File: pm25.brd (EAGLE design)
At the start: 55.9 x 33 mm, 33 parts, among them J1 CON-0024, Q1 TRANSISTOR-NPN-40V-0.2A-SOT23, Q2 TR-0001, U1 IC-0010, U2 CCS811B-JOPD500, U3 POWER-SWITCH-SIP32509DT', U4 SI7021-A20-GM1R

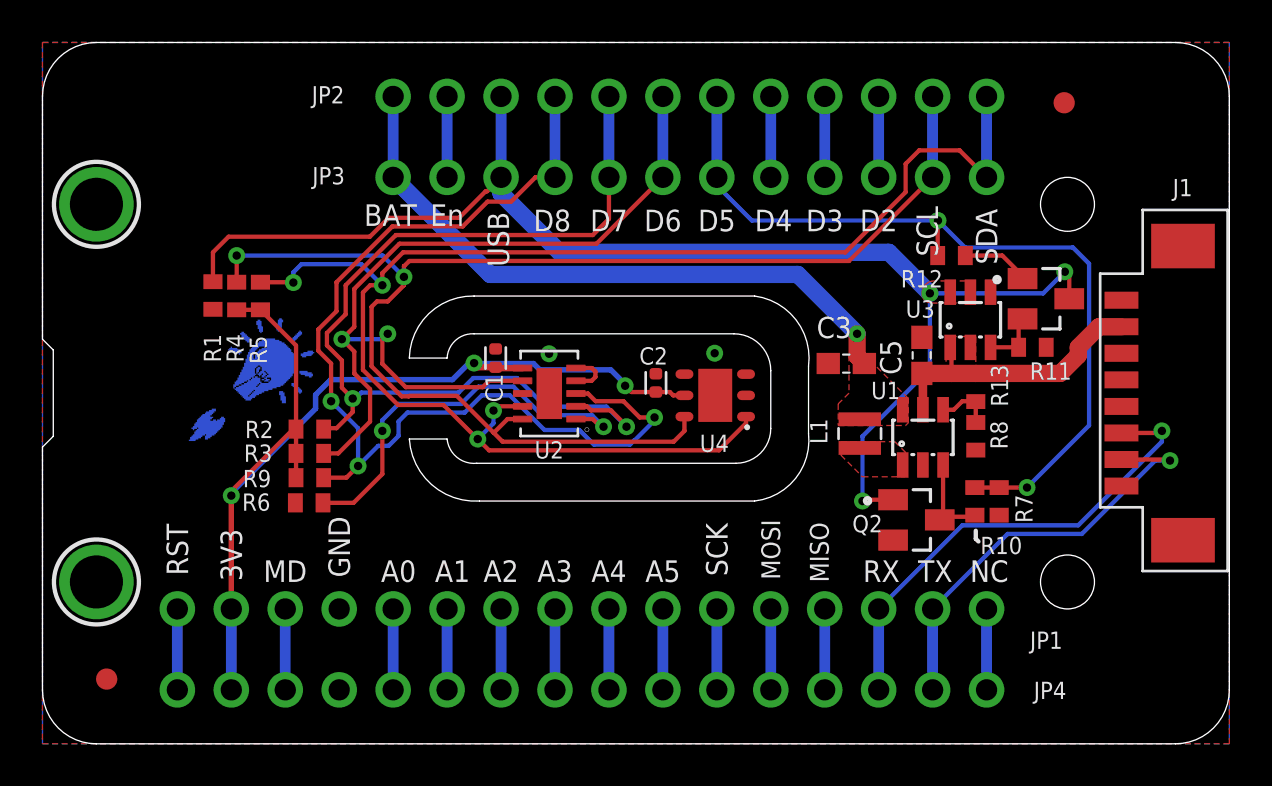
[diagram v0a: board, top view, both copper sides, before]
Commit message: Slight hardware update. Substitute MCP1640 on U1 Add L2 Add TP1
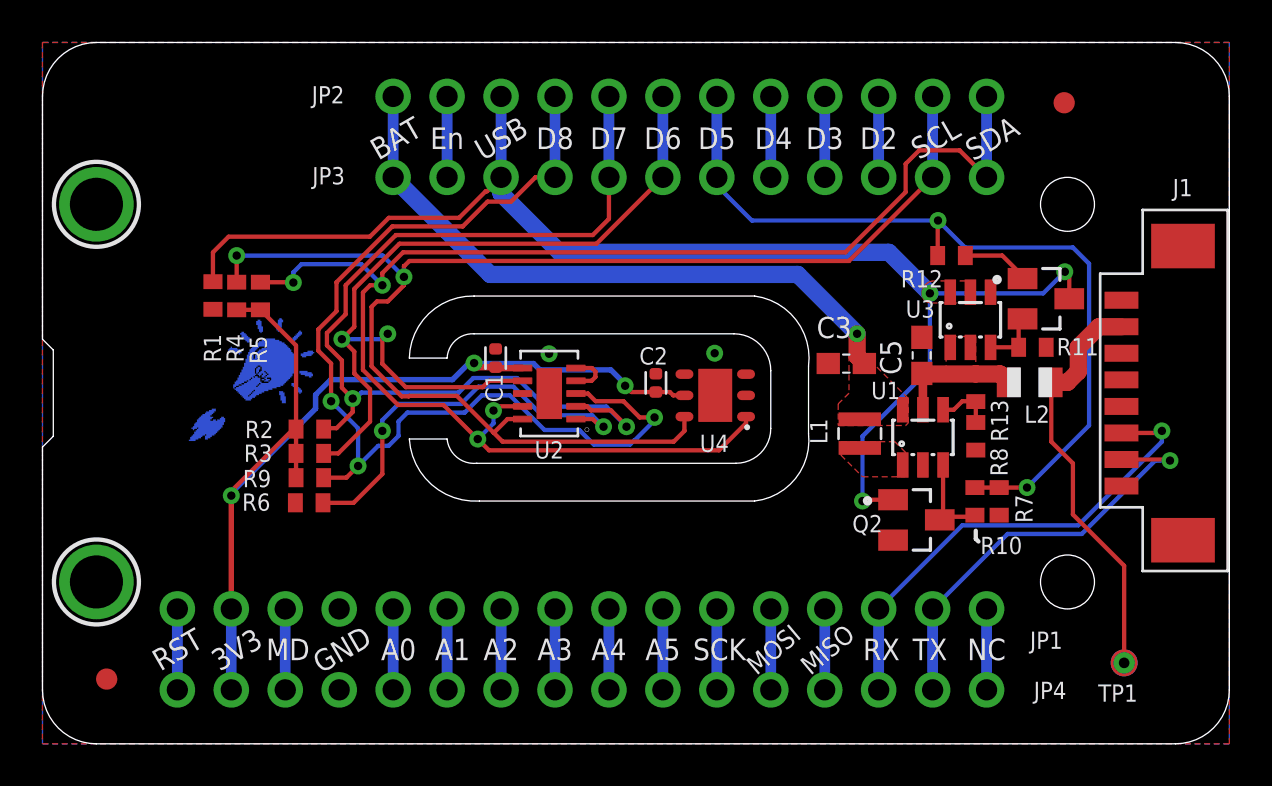
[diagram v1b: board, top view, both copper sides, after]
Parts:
- added L2: 2k, wolff-den:R0805
- added TP1: TP, wolff-den:TP-1P27
- U1: value IC-0010 -> POWER-VREG-FB-EN-SW-350MA
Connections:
- new net V5V0_BEAD: C5.1, L2.1, R13.2, U1.5, U3.1, U3.2
- net V5V0_HAT: now also L2.2, TP1.P$1, TP1.P$2, TP1.TP; no longer C5.1, R13.2, U1.5, U3.1, U3.2
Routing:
- net V5V0_HAT: track 13.6 -> 19.7 mm
- net V5V0_BEAD: track 0.00 -> 5.94 mm
- added copper zone on layer 1, net V5V0_BEAD
- removed copper zone on layer 1, net V5V0_HAT
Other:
- board text added: ">LAST_DATE_TIME"
- board text added: "BRD-0010-02"
- board text removed: "BRD-0010-01"

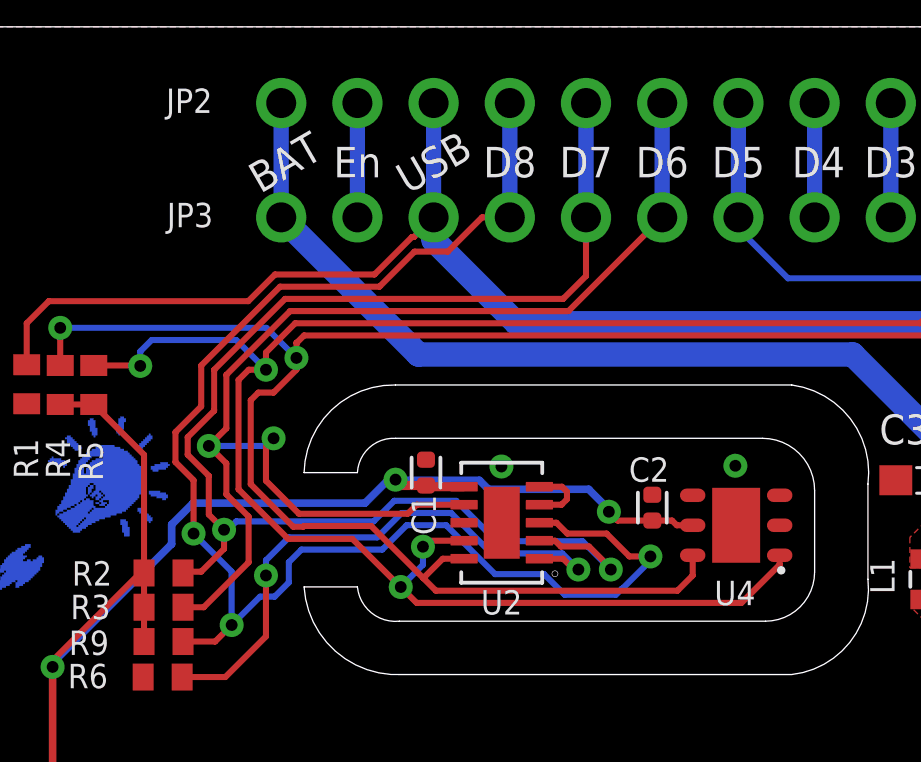
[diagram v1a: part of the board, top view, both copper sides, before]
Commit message: Replacing connection from D7 with D5 (so the LED isn't always on)
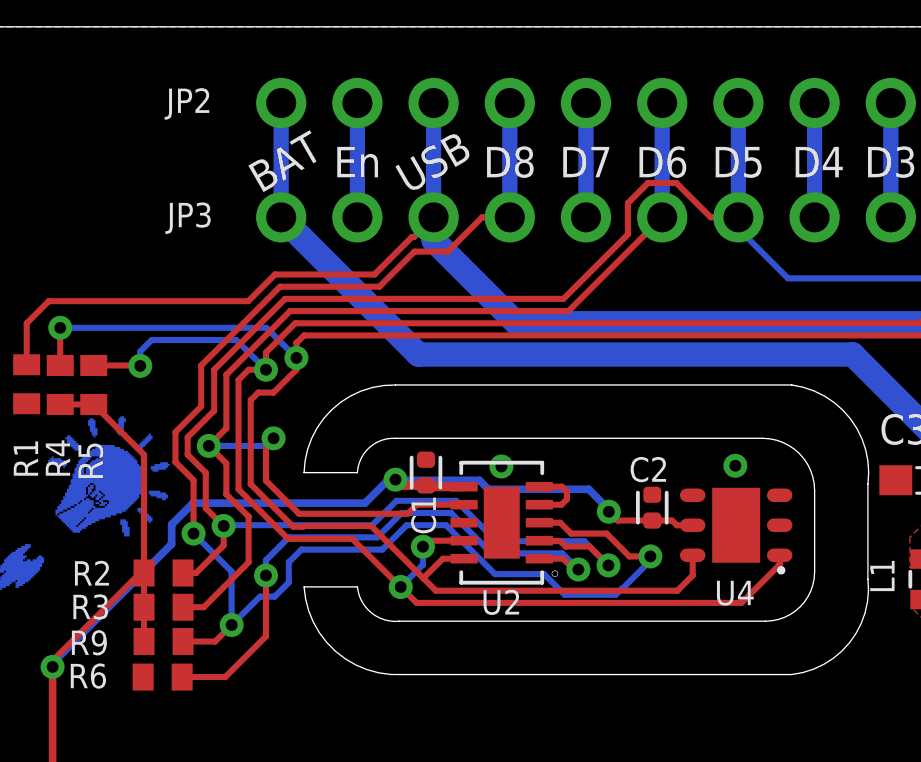
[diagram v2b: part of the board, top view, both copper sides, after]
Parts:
- added PCB1: PCB-PS-CCS811-SI7021, wolff-den:PLACEHOLDER
- U3: value POWER-SWITCH-SIP32509DT' -> POWER-SWITCH-SIP32509DT
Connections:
- net D5: now also R2.1, U2.2
- net D7: no longer R2.1, U2.2
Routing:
- net D5: track 39.1 -> 85.4 mm, vias 2 -> 4
- net D7: track 45.0 -> 3.81 mm, vias 2 -> 0

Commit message: Fixing issue with intermittent BOOST/USB control.
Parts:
- added Q3: TR-0003, wolff-den:SOT23
- Q1: value TRANSISTOR-NPN-40V-0.2A-SOT23 -> TR-0001
- R11: value 100k -> 1k
- R12: value 1k -> 100k
- moved Q1 7.78 mm to (39.5, 21.7), turned to 0 degrees
- moved R11 2.11 mm to (47.8, 16.9), turned to 90 degrees
- moved L2 1.09 mm to (45.8, 16.1), turned to 270 degrees
- moved R12 0.40 mm to (42.7, 22.6), turned to 180 degrees
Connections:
- net D5: now also Q1.1; no longer R12.1
- net GND: now also J1.1, Q1.2; no longer J1.8
- net N$3: now also Q1.3, Q3.1, R12.1; no longer Q1.2, R11.2, U3.3
- net N$7: now also Q3.3, R11.2, U3.3; no longer Q1.1, R12.2
- net RX: now also J1.3; no longer J1.6
- net TX: now also J1.2; no longer J1.7
- net V5V0_HAT: now also J1.7; no longer J1.2
- net VBUS: now also Q3.2, R12.2; no longer Q1.3
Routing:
- net N$3: track 2.74 -> 10.9 mm
- net TX: track 20.3 -> 26.2 mm
- net RX: track 22.9 -> 26.3 mm
- net V5V0_HAT: track 19.7 -> 16.3 mm
- net VBUS: track 64.0 -> 63.2 mm
- net N$7: track 3.22 -> 3.89 mm
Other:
- board text added: "BRD-0010-03"
- board text removed: "BRD-0010-02"

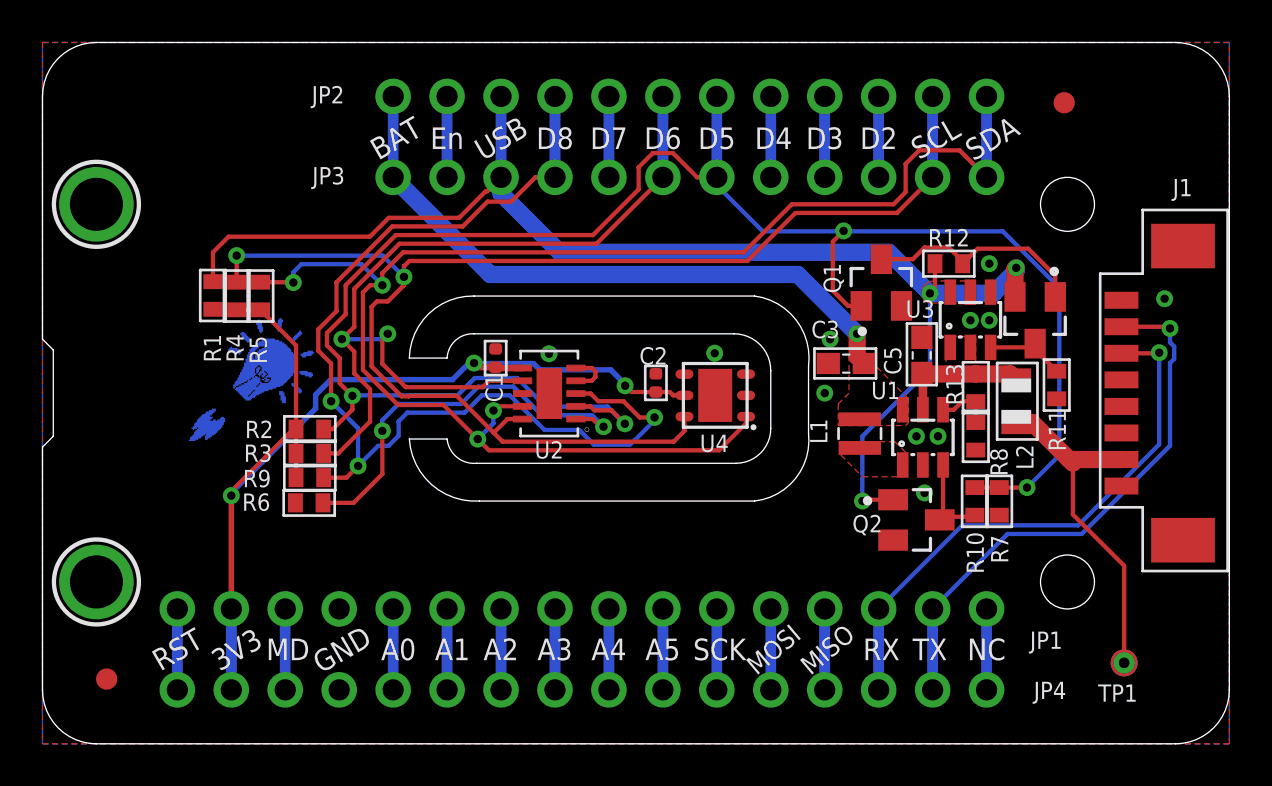
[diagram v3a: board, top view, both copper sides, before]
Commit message: Updating board based on recommendations
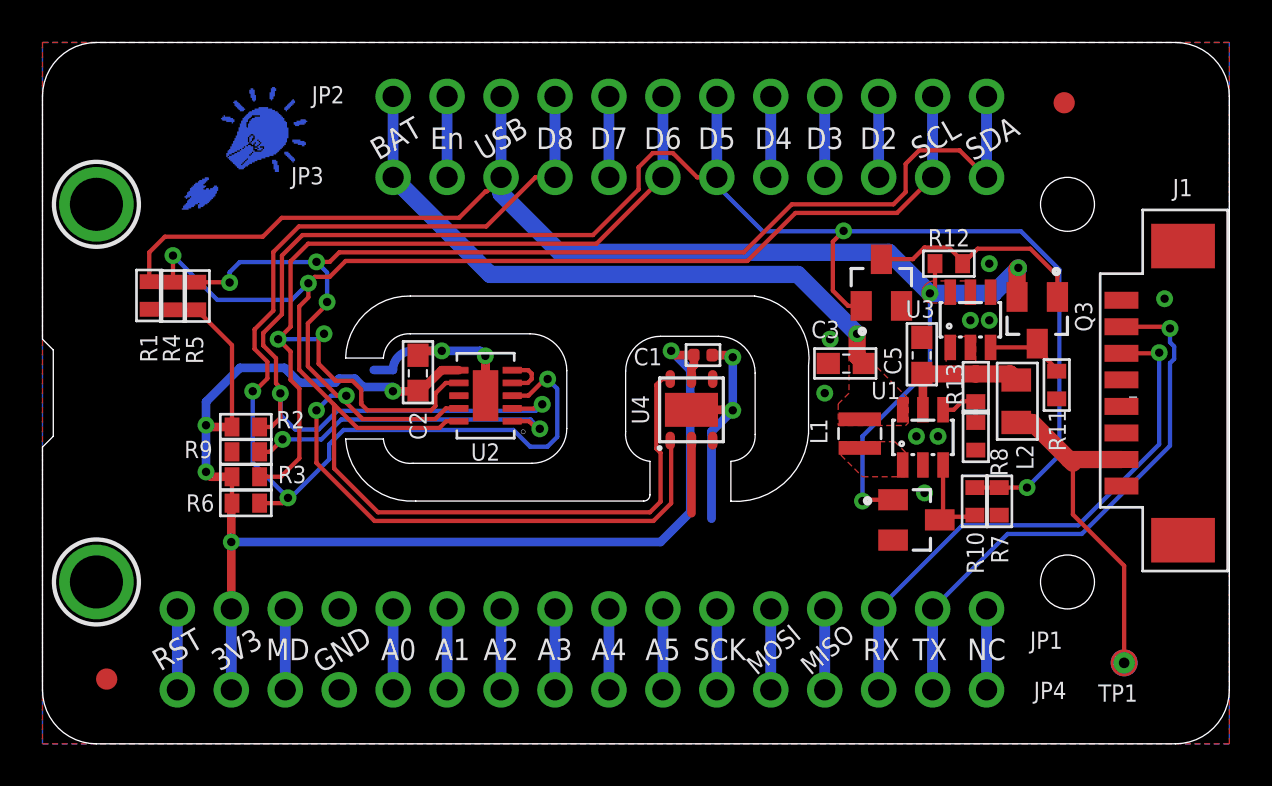
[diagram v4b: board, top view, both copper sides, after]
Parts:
- added U$1: (no value), wolff-den:LOGO-CIRCUITDOJO-BULB
- added U$2: (no value), wolff-den:LOGO-CIRCUITDOJO
- C2: value 0.1u -> 4.7u; device wolff-den:CAPC1005X55N -> wolff-den:C0603
- R2, R3, R6, R9: value 100k -> 4.7k
- moved C2 11.2 mm to (17.7, 17.4)
- moved C1 9.76 mm to (31.1, 18.3), turned to 0 degrees
- moved R9 3.83 mm to (9.57, 13.7)
- moved R6 3.25 mm to (9.57, 11.3)
- moved R3 3.21 mm to (9.57, 12.6)
- moved R2 3.02 mm to (9.57, 14.9)
- moved U2 3.00 mm to (20.9, 16.4)
- moved R1 3.00 mm to (5.03, 21.1)
- moved R4 3.00 mm to (6.14, 21.1)
- moved R5 3.00 mm to (7.26, 21.1)
- moved U4 1.31 mm to (30.6, 15.7), turned to 90 degrees
- moved Q3 0.10 mm to (46.8, 19.9)
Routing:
- net GND: track 0.00 -> 24.4 mm, vias 11 -> 13
- net +3V3: track 50.8 -> 69.5 mm, vias 3 -> 5
- net SCL: track 64.4 -> 82.9 mm
- net SDA: track 71.6 -> 84.5 mm, vias 4 -> 5
- net D6: track 41.3 -> 47.7 mm
- net N$4: track 19.2 -> 15.5 mm
- net D8: track 49.4 -> 53.0 mm
- net VBUS: track 63.2 -> 66.2 mm
- net D5: track 85.8 -> 88.7 mm
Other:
- outline, holes or cut-outs redrawn
- board text added: "BRD-0010-04"
- board text removed: "BRD-0010-03"

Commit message: Fixing load switch option
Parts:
- U3: value POWER-SWITCH-SIP32509DT -> POWER-SWITCH-SIP32508-SO23-6
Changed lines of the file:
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@@
 <drawing>
 <settings>
-<setting alwaysvectorfont="yes"/>
+<setting alwaysvectorfont="no"/>
 <setting keepoldvectorfont="yes"/>
 <setting verticaltext="up"/>
@@
 <attribute name="VALUE" x="45.72" y="5.715" size="0.4064" layer="27" ratio="10" rot="R180"/>
 </element>
-<element name="U1" library="wolff-den" library_urn="urn:adsk.eagle:library:6370453" package="SOT23-6" package3d_urn="urn:adsk.eagle:package:5807329/2" value="POWER-VREG-FB-EN-SW-350MA" x="41.4528" y="14.4272" smashed="yes">
+<element name="U1" library="wolff-den" library_urn="urn:adsk.eagle:library:6370453" package="SOT23-6" package3d_urn="urn:adsk.eagle:package:5807329/3" value="POWER-VREG-FB-EN-SW-350MA" x="41.4528" y="14.4272" smashed="yes">
 <attribute name="DIGIKEYPN" value="MCP1640BT-I/CHYCT-ND" x="41.4528" y="14.4272" size="1.778" layer="27" display="off"/>
 <attribute name="MPN" value="MCP1640BT-I/CHY" x="41.4528" y="14.4272" size="1.778" layer="27" display="off"/>
@@
 <attribute name="DIGIKEYPN" value="1727-1142-1-ND" x="41.148" y="10.541" size="1.778" layer="27" rot="R270" display="off"/>
 <attribute name="MPN" value="BSS138P,215" x="41.148" y="10.541" size="1.778" layer="27" rot="R270" display="off"/>
+<attribute name="NAME" x="40.753" y="10.946" size="0.8128" layer="51" rot="R270"/>
 <attribute name="NAME" x="38.1254" y="9.9568" size="0.8128" layer="25"/>
-<attribute name="NAME" x="40.753" y="10.946" size="0.8128" layer="51" rot="R270"/>
 <attribute name="TEMPHIGH" value="150" x="41.148" y="10.541" size="1.778" layer="27" rot="R270" display="off"/>
 <attribute name="TEMPLOW" value="-55" x="41.148" y="10.541" size="1.778" layer="27" rot="R270" display="off"/>
@@
 <attribute name="VENDOR" value="Yageo" x="7.2616" y="21.082" size="1.778" layer="27" rot="R270" display="off"/>
 </element>
-<element name="U3" library="wolff-den" library_urn="urn:adsk.eagle:library:6370453" package="SOT23-6" package3d_urn="urn:adsk.eagle:package:5807329/2" value="POWER-SWITCH-SIP32509DT" x="43.688" y="19.9644" smashed="yes">
+<element name="U3" library="wolff-den" library_urn="urn:adsk.eagle:library:6370453" package="SOT23-6" package3d_urn="urn:adsk.eagle:package:5807329/3" value="POWER-SWITCH-SIP32508-SO23-6" x="43.688" y="19.9644" smashed="yes">
 <attribute name="DESC" value="IC LOAD SWITCH SOT23-6" x="43.688" y="19.9644" size="1.778" layer="27" display="off"/>
-<attribute name="DIGIKEYPN" value="SIP32509DT-T1-GE3CT-ND" x="43.688" y="19.9644" size="1.778" layer="27" display="off"/>
-<attribute name="MPN" value="SIP32509DT-T1-GE3" x="43.688" y="19.9644" size="1.778" layer="27" display="off"/>
+<attribute name="DIGIKEYPN" value="SIP32508DT-T1-GE3CT-ND" x="43.688" y="19.9644" size="1.778" layer="27" display="off"/>
+<attribute name="MPN" value="SIP32508DT-T1-GE3" x="43.688" y="19.9644" size="1.778" layer="27" display="off"/>
 <attribute name="NAME" x="40.64" y="20.066" size="0.8128" layer="25"/>
 </element>
@@
 <attribute name="DIGIKEYPN" value="1727-1142-1-ND" x="39.497" y="21.717" size="1.778" layer="27" display="off"/>
 <attribute name="MPN" value="BSS138P,215" x="39.497" y="21.717" size="1.778" layer="27" display="off"/>
+<attribute name="NAME" x="39.092" y="21.322" size="0.8128" layer="51"/>
 <attribute name="NAME" x="37.592" y="21.209" size="0.8128" layer="25" rot="R90"/>
-<attribute name="NAME" x="39.092" y="21.322" size="0.8128" layer="51"/>
 <attribute name="TEMPHIGH" value="150" x="39.497" y="21.717" size="1.778" layer="27" display="off"/>
 <attribute name="TEMPLOW" value="-55" x="39.497" y="21.717" size="1.778" layer="27" display="off"/>
@@
 <attribute name="DIGIKEYPN" value="BSS84-FDICT-ND" x="46.836" y="19.939" size="1.778" layer="27" rot="R180" display="off"/>
 <attribute name="MPN" value="BSS84-7-F" x="46.836" y="19.939" size="1.778" layer="27" rot="R180" display="off"/>
+<attribute name="NAME" x="48.614" y="20.828" size="0.8128" layer="25" rot="R270"/>
 <attribute name="NAME" x="47.241" y="20.334" size="0.8128" layer="51" rot="R180"/>
-<attribute name="NAME" x="48.614" y="20.828" size="0.8128" layer="25" rot="R270"/>
 <attribute name="TEMPHIGH" value="150" x="46.836" y="19.939" size="1.778" layer="27" rot="R180" display="off"/>
 <attribute name="TEMPLOW" value="-55" x="46.836" y="19.939" size="1.778" layer="27" rot="R180" display="off"/>
@@
 <wire x1="17.8862" y1="18.5" x2="18.8" y2="18.5" width="0.4064" layer="1"/>
 <via x="18.8" y="18.5" extent="1-16" drill="0.3937"/>
+<wire x1="52.832" y1="20.955" x2="50.8" y2="20.885" width="0" layer="19" extent="1-1"/>
+<wire x1="47.752" y1="16.241" x2="50.8" y2="20.885" width="0" layer="19" extent="1-1"/>
+<wire x1="43.942" y1="13.828" x2="47.752" y2="16.241" width="0" layer="19" extent="1-1"/>
+<wire x1="42.164" y1="14.478" x2="43.942" y2="13.828" width="0" layer="19" extent="1-1"/>
+<wire x1="41.148" y1="14.478" x2="42.164" y2="14.478" width="0" layer="19" extent="1-1"/>
+<wire x1="41.4528" y1="13.1272" x2="41.148" y2="14.478" width="0" layer="19" extent="1-1"/>
+<wire x1="41.529" y1="11.811" x2="41.4528" y2="13.1272" width="0" layer="19" extent="1-1"/>
+<wire x1="40.048" y1="9.591" x2="41.529" y2="11.811" width="0" layer="19" extent="1-1"/>
+<wire x1="45.042" y1="10.765" x2="43.942" y2="13.828" width="0" layer="19" extent="1-1"/>
+<wire x1="41.402" y1="19.138" x2="41.148" y2="14.478" width="0" layer="19" extent="1-1"/>
+<wire x1="40.447" y1="20.617" x2="41.402" y2="19.138" width="0" layer="19" extent="1-1"/>
+<wire x1="43.688" y1="19.939" x2="41.402" y2="19.138" width="0" layer="19" extent="1-1"/>
+<wire x1="44.577" y1="19.939" x2="43.688" y2="19.939" width="0" layer="19" extent="1-1"/>
+<wire x1="44.638" y1="21.2644" x2="44.577" y2="19.939" width="0" layer="19" extent="1-1"/>
+<wire x1="44.577" y1="22.606" x2="44.638" y2="21.2644" width="0" layer="19" extent="1-1"/>
+<wire x1="37.084" y1="19.05" x2="40.447" y2="20.617" width="0" layer="19" extent="1-1"/>
+<wire x1="36.996" y1="17.907" x2="37.084" y2="19.05" width="0" layer="19" extent="1-1"/>
+<wire x1="36.83" y1="16.51" x2="36.996" y2="17.907" width="0" layer="19" extent="1-1"/>
+<wire x1="32.5" y1="15.7" x2="36.83" y2="16.51" width="0" layer="19" extent="1-1"/>
+<wire x1="30.5558" y1="10.8558" x2="31.5" y2="10.6" width="0" layer="19" extent="1-16"/>
+<wire x1="20.861" y1="16.3908" x2="30.5558" y2="15.724" width="0" layer="19" extent="1-1"/>
+<wire x1="8.923" y1="13.746" x2="15.6" y2="17.6" width="0" layer="19" extent="1-16"/>
+<wire x1="5.0264" y1="20.4574" x2="8.923" y2="13.746" width="0" layer="19" extent="1-1"/>
+<wire x1="13.97" y1="6.35" x2="8.923" y2="13.746" width="0" layer="19" extent="1-1"/>
+<wire x1="13.97" y1="2.54" x2="13.97" y2="6.35" width="0" layer="19" extent="1-1"/>
 </signal>
 <signal name="MOSI">
@@
 <wire x1="44.77385" y1="21.209" x2="45.947" y2="22.38215" width="0.8128" layer="16"/>
 <wire x1="45.947" y1="22.38215" x2="45.947" y2="22.40915" width="0.8128" layer="16"/>
+<wire x1="42.738" y1="21.2644" x2="43.688" y2="21.2644" width="0" layer="19" extent="1-1"/>
+<wire x1="41.783" y1="21.209" x2="42.738" y2="21.2644" width="0" layer="19" extent="1-1"/>
 </signal>
 <signal name="MD">
@@
 <vertex x="37.973" y="16.51"/>
 </polygon>
+<wire x1="38.481" y1="15.28" x2="40.5028" y2="15.7272" width="0" layer="19" extent="1-1"/>
+<wire x1="38.696" y1="17.907" x2="38.481" y2="15.28" width="0" layer="19" extent="1-1"/>
 </signal>
 <signal name="D3">
@@
 <vertex x="40.132" y="14.224"/>
 </polygon>
+<wire x1="40.5028" y1="13.1272" x2="38.481" y2="13.93" width="0" layer="19" extent="1-1"/>
 </signal>
 <signal name="N$4">
@@
 <wire x1="43.942" y1="17.414" x2="45.562" y2="17.414" width="0.8128" layer="1"/>
 <wire x1="45.562" y1="17.414" x2="45.847" y2="17.129" width="0.8128" layer="1"/>
+<wire x1="42.738" y1="18.6644" x2="43.688" y2="18.6644" width="0" layer="19" extent="1-1"/>
+<wire x1="43.942" y1="17.414" x2="43.688" y2="18.6644" width="0" layer="19" extent="1-1"/>
 </signal>
 <signal name="N$3">

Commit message: Renaming to Air Quality Wing
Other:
- board text added: "Air Quality Wing"
- board text removed: "2"
- board text removed: "Particle"
